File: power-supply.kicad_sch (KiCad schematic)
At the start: 17 parts

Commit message: fully move to new MCU configuration
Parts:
- removed R? (x2): 1K, SamacSys_Parts:RESC2012X60N, symbol SamacSys_Parts:SG73P2ATTD102J
- added R10: 10k, SamacSys_Parts:RESC5025X65N, symbol SamacSys_Parts:RC2010JK-0710KL
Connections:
- net +5V: now also R10.1
- net at IC?.5 (EN): now also R10.2

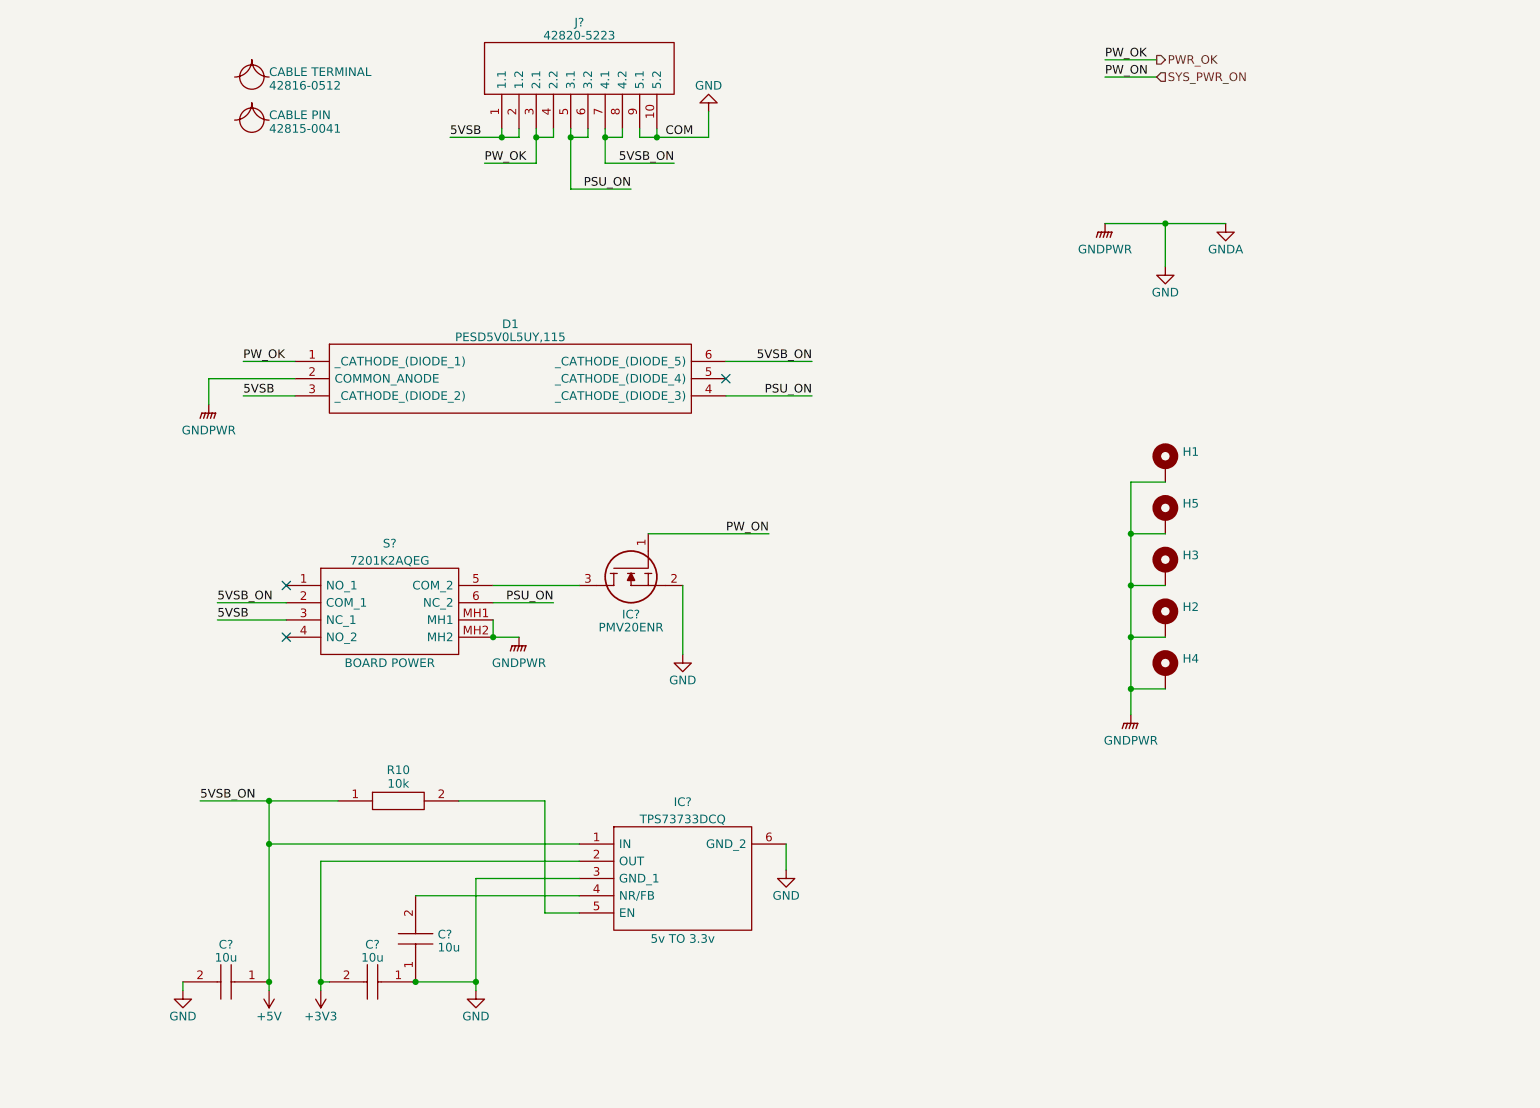
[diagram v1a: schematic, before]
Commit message: first few boards laid out
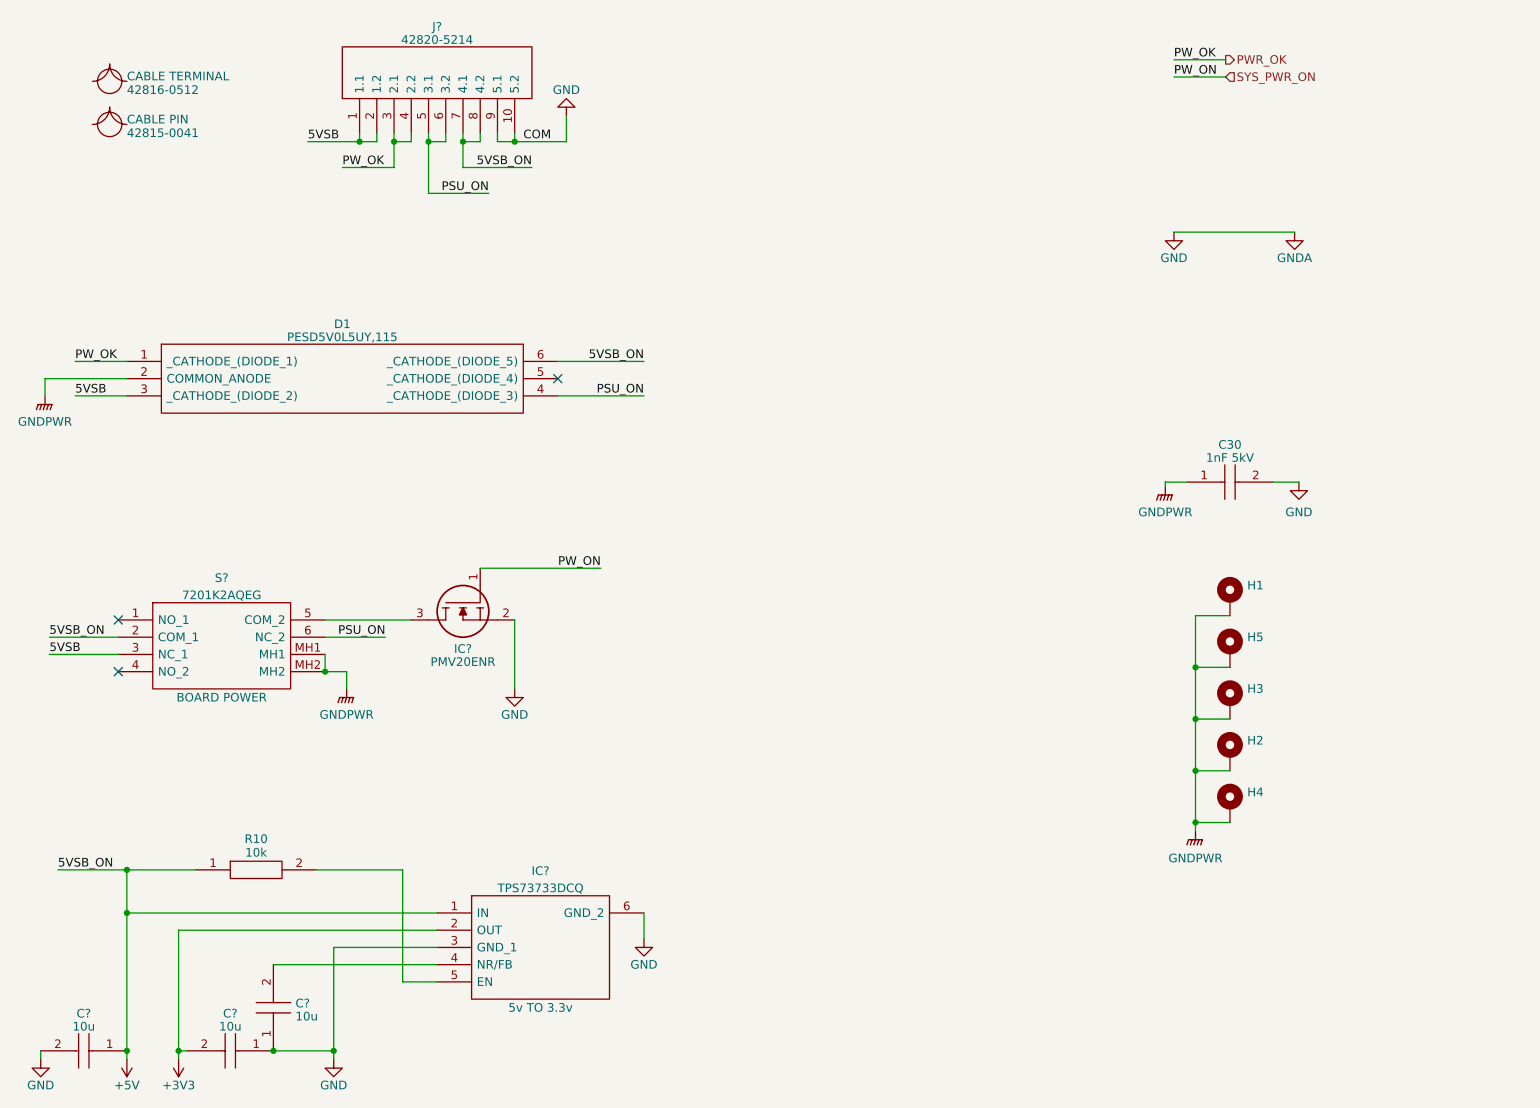
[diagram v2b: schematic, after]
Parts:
- removed J?: 42820-5223, SamacSys_Parts:42820-5XXY_1, symbol SamacSys_Parts:42820-5223
- added C30: 1nF 5kV, CAPC5664X270N, symbol SamacSys_Parts:HV2225Y102KXMATHV
- added J?: 42820-5214, 42820-5XXY_1, symbol SamacSys_Parts:42820-5223
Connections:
- net +5V: now also J?.7 (4.1), J?.8 (4.2)
- net 5VSB: now also J?.1 (1.1), J?.2 (1.2)
- net GND: now also C30.2, J?.10 (5.2), J?.9 (5.1); no longer D1.2 (COMMON_ANODE), H1.1, H2.1, H3.1, H4.1, H5.1, S?.MH1, S?.MH2
- net PSU_ON: now also J?.5 (3.1), J?.6 (3.2)
- net PWR_OK: now also J?.3 (2.1), J?.4 (2.2)
- new net GNDPWR: C30.1, D1.2 (COMMON_ANODE), H1.1, H2.1, H3.1, H4.1, H5.1, S?.MH1, S?.MH2
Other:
- moved on the sheet: C?, D1, H1, H2, H3, H4, H5, IC?, R10, S?

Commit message: first panelization of entire modular dev board
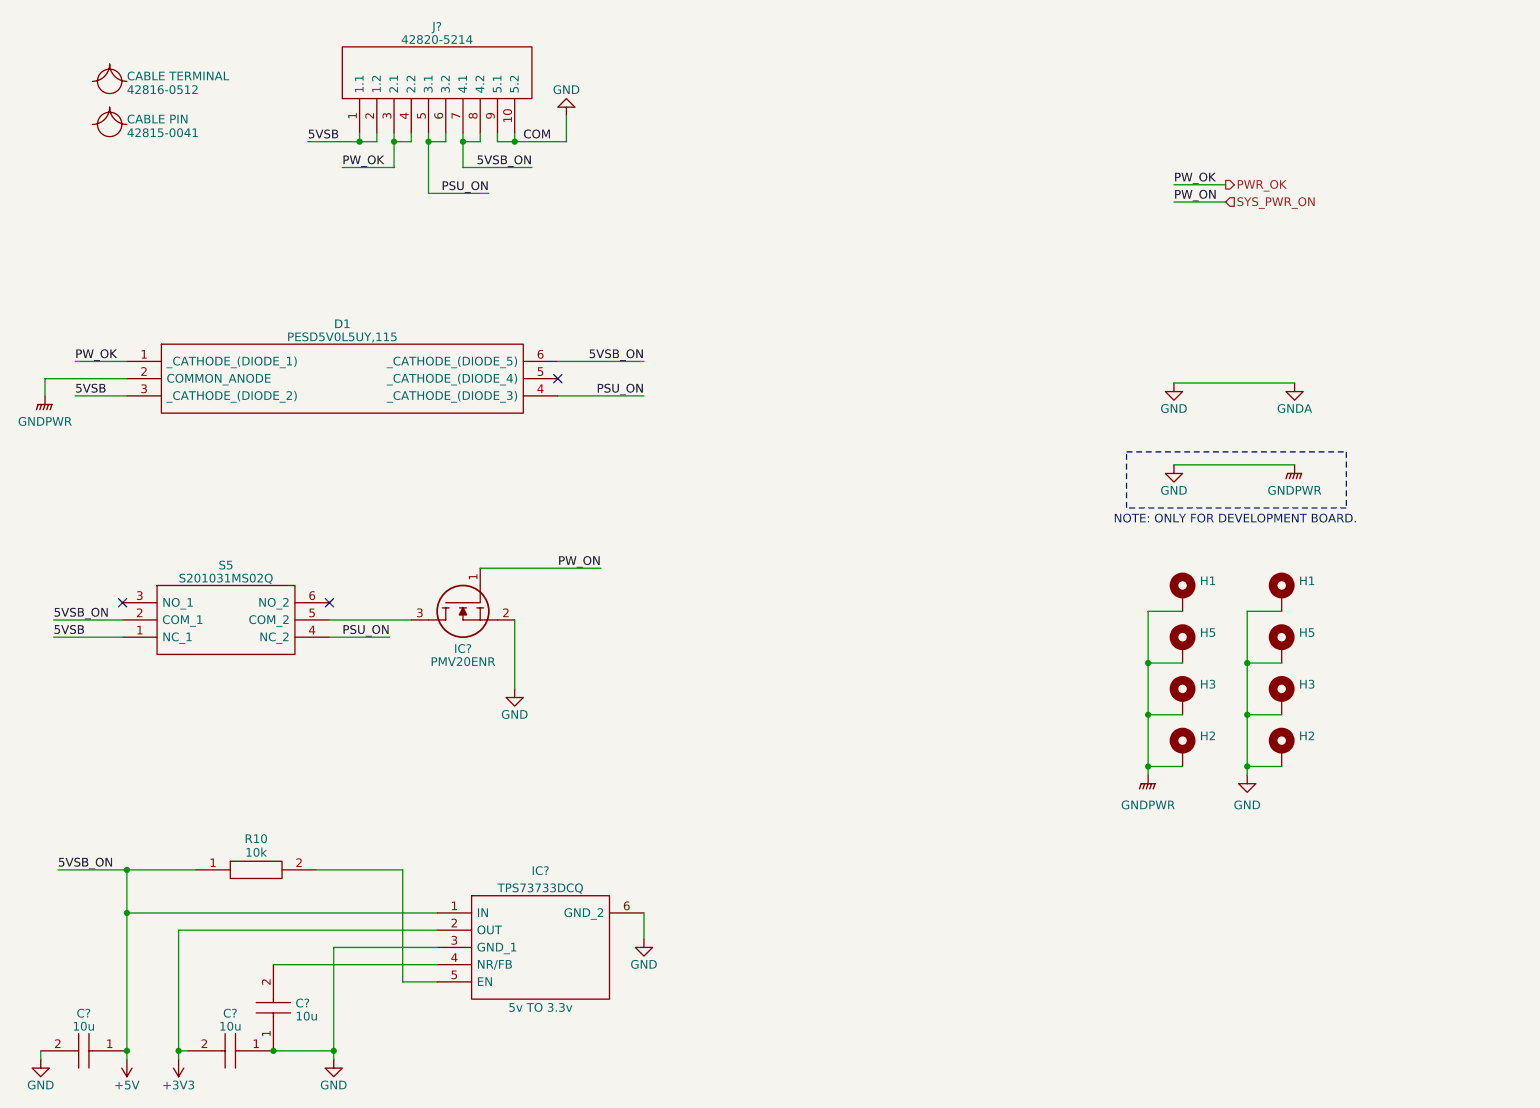
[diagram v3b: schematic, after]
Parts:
- removed C30: 1nF 5kV, CAPC5664X270N, symbol SamacSys_Parts:HV2225Y102KXMATHV
- removed H4: MountingHole_Pad, MountingHole:MountingHole_3.2mm_M3_Pad_Via, symbol Mechanical:MountingHole_Pad
- removed S?: 7201K2AQEG, SamacSys_Parts:7201K2AQEG, symbol SamacSys_Parts:7201K2AQEG
- added H1, H2, H3, H5: MountingHole_Pad, MountingHole:MountingHole_3.2mm_M3_Pad_Via, symbol Mechanical:MountingHole_Pad
- added S5: S201031MS02Q, S201031MS02Q, symbol SamacSys_Parts:S201031MS02Q
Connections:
- net GNDPWR is gone; now on net GND: D1.2 (COMMON_ANODE), H1.1, H2.1, H3.1, H5.1
- net +5V: now also S5.2 (COM_1)
- net 5VSB: now also S5.1 (NC_1)
- net GND: now also H1.1, H2.1, H3.1, H5.1
- net PSU_ON: now also S5.4 (NC_2)
- net at IC?.3: now also S5.5 (COM_2)
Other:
- note added: "NOTE: ONLY FOR DEVELOPMENT BOARD."
- moved on the sheet: H1, H2, H3, H5

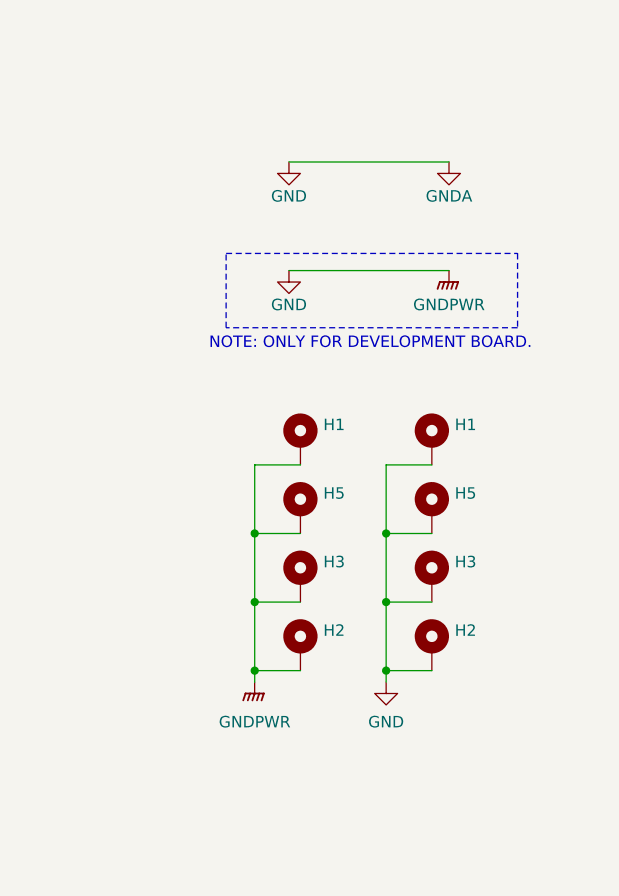
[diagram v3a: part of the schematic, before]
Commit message: use GND instead of GNDA
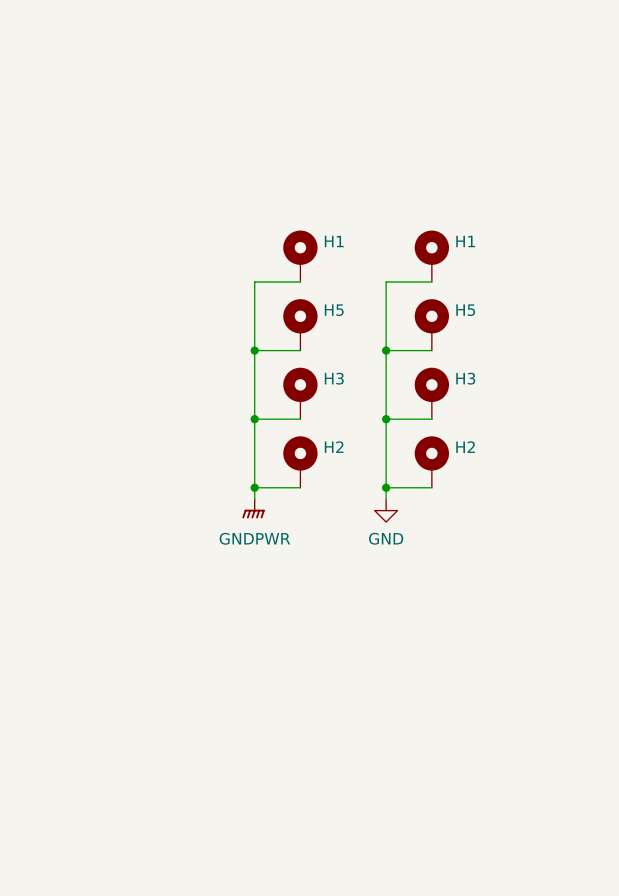
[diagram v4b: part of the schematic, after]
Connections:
- net GND: no longer D1.2 (COMMON_ANODE), H1.1, H2.1, H3.1, H5.1
- new net GNDPWR: D1.2 (COMMON_ANODE), H1.1, H2.1, H3.1, H5.1
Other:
- note removed: "NOTE: ONLY FOR DEVELOPMENT BOARD."
- moved on the sheet: H1, H2, H3, H5

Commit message: initial board layout
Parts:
- removed H1 (x2), H3, H5: MountingHole_Pad, MountingHole:MountingHole_3.2mm_M3_Pad_Via, symbol Mechanical:MountingHole_Pad
- removed S5: S201031MS02Q, S201031MS02Q, symbol SamacSys_Parts:S201031MS02Q
- added H5 (x2): MountingHole_Pad, MountingHole:MountingHole_3.2mm_M3_Pad_Via, symbol Mechanical:MountingHole_Pad
- added S2: MSS225004, MSS225004, symbol SamacSys_Parts:MSS225004
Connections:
- net +5V: now also S2.1
- net 5VSB: now also S2.2
- net GNDPWR: now also H5.1, H5.1, S2.MH1, S2.MH2, S2.MH3, S2.MH4
- net PSU_ON: now also S2.4
- net at IC?.3: now also S2.5
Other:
- moved on the sheet: C?, D1, H2, H3, H5, IC?, J?, R10
